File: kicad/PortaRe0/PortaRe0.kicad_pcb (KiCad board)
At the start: 4 copper layers, 135 x 77 mm, 355 parts, among them CN1 M.2, J1 StickSocket, J2 SPK_R, J3 SPK_L, J4 Battery, J6 Fan, J9 PJ-307C, Q1 BSS138, SW1 SW_START, SW2 KillSW, U1 BQ25895RTWR, U10 TPS2042BDR, U11 RP2040#2, U12 HC-USB3.0-L168-WP, U13 PCM5102APWR, U14 TPA6132A2RTER, U15 MAX98357AEWL+T_R, U16 RT9080-33GJ5, U2 TPS61023DRLR, U3 AP2112K-3.3TRG1, U4 VL812, U5 W25Q32JVSSIQ, U6 RP2040#1, U7 TPS61023DRLR, U8 USB31-TYPE-C-FSABC, U9 MAX98357AEWL+T_L, Y1 C9006, Y2 C70565, Y4 C70565

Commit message: Docs: session33終了処理・J4コネクタ確定・pcb_layout_notes作成
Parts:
- removed J4: Battery, PortaRe0:CONN-TH_S8B-PH-K-S-LF-SN
- removed K_SW65: BOOTSEL_SW, PortaRe0:KEY-SMD_4P-L4.2-W3.2-P2.20-LS4.6
- added B_SW1: BOOTSEL_SW, PortaRe0:KEY-SMD_4P-L4.2-W3.2-P2.20-LS4.6, B.Cu at (214.9, 182.4)
- added B_SW2: BOOTSEL_SW, PortaRe0:KEY-SMD_4P-L4.2-W3.2-P2.20-LS4.6, B.Cu at (222.6, 182.9)
- added SW_D64: 1N4148W, PortaRe0:SOD-123_L2.8-W1.8-LS3.7-RD, F.Cu at (241.0, 168.3)
- added Stick1: 5034800440, PortaRe0:FPC-SMD_5034800400, B.Cu at (237.7, 165.0)
- C1, C10, C100, C101, C102, C103, C104, C105, C106, C107, C108, C109, C11, C110, C111, C112, C113, C114, C115, C116, C117, C118, C119, C12, C13, C14, C15, C16, C17, C18, C19, C2, C20, C21, C22, C23, C24, C25, C26, C27, C28, C29, C3, C30, C31, C32, C33, C34, C36, C38, C4, C41, C42, C44, C46, C47, C48, C49, C5, C50, C51, C52, C53, C54, C55, C56, C57, C58, C59, C6, C60, C61, C62, C63, C64, C65, C66, C67, C68, C69, C7, C70, C71, C72, C73, C74, C75, C76, C77, C78, C79, C8, C80, C81, C82, C83, C84, C85, C86, C87, C88, C89, C9, C90, C91, C92, C93, C94, C95, C96, C97, C98, C99, CN1, D5, D6, D7, D8, D9, FPC2, FPC4, FPC5, FPC6, J2, J3, J6, J9, L1, L2, L3, L4, Q1, R1, R10, R11, R12, R13, R14, R15, R16, R17, R18, R19, R2, R20, R21, R22, R23, R24, R25, R26, R27, R28, R29, R3, R30, R31, R32, R33, R34, R35, R36, R37, R38, R39, R4, R40, R41, R42, R43, R44, R45, R46, R47, R48, R49, R5, R50, R51, R52, R53, R54, R55, R56, R57, R58, R59, R6, R60, R61, R62, R63, R64, R7, R8, R9, RP2040#1, RP2040#2, SW1, SW2, U1, U10, U11, U12, U13, U14, U15, U16, U2, U3, U4, U5, U6, U7, U8, U9, USBC1, Y1, Y2, Y4: moved to B.Cu
- J1: value StickSocket -> Battery; footprint PortaRe0:FPC-SMD_5034800400 -> PortaRe0:CONN_BM06B-ACHFKS-GACN-ETF_JST; moved to B.Cu
- K_SW64: value BOOTSEL_SW -> KeyBoard
- moved SW_D2 264.3 mm to (280.0, 108.0)
- moved K_SW17 263.2 mm to (277.0, 122.7)
- moved K_SW31 261.5 mm to (275.8, 135.5)
- moved SW_D17 257.3 mm to (277.0, 125.7), turned to 180 degrees
- moved K_SW16 256.6 mm to (268.5, 122.7)
- moved SW_D31 251.5 mm to (275.5, 138.5), turned to 180 degrees
- moved K_SW30 251.0 mm to (264.0, 131.2)
- moved K_SW15 250.1 mm to (260.0, 122.7)
- moved K_SW57 250.0 mm to (272.4, 148.2)
- moved SW_D16 249.6 mm to (268.5, 125.7), turned to 180 degrees
- moved K_SW14 243.8 mm to (251.5, 122.7)
- moved SW_D57 243.2 mm to (272.4, 151.2), turned to 180 degrees
- moved SW_D15 242.1 mm to (260.0, 125.7), turned to 180 degrees
- moved K_SW44 241.5 mm to (266.0, 139.7)
- moved SW_D30 239.8 mm to (263.8, 134.2), turned to 180 degrees
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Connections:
- J1 pad 1: GND -> +BATT
- J1 pad 2: STICK_X -> +BATT
- J1 pad 3: +3V3 -> +BATT
- J1 pad 4: STICK_Y -> GND
- J1 pad 5: (no net) -> GND
- J1 pad 6: (no net) -> GND
- K_SW1 pad 2: /keyboard/COL0 -> unconnected-(K_SW1-Pad2)
- K_SW1 pad 3: (no net) -> /keyboard/COL0
- K_SW1 pad 4: (no net) -> unconnected-(K_SW1-Pad4)
- K_SW10 pad 1: Net-(SW_D10-A) -> /keyboard/COL7
- K_SW10 pad 2: /keyboard/COL7 -> unconnected-(K_SW10-Pad2)
- K_SW10 pad 3: (no net) -> Net-(SW_D10-A)
- K_SW10 pad 4: (no net) -> unconnected-(K_SW10-Pad4)
- K_SW11 pad 1: Net-(SW_D11-A) -> /keyboard/COL8
- K_SW11 pad 2: /keyboard/COL8 -> unconnected-(K_SW11-Pad2)
- K_SW11 pad 3: (no net) -> Net-(SW_D11-A)
- K_SW11 pad 4: (no net) -> unconnected-(K_SW11-Pad4)
- K_SW12 pad 1: Net-(SW_D12-A) -> /keyboard/COL0
- K_SW12 pad 2: /keyboard/COL0 -> unconnected-(K_SW12-Pad2)
- K_SW12 pad 3: (no net) -> Net-(SW_D12-A)
- K_SW12 pad 4: (no net) -> unconnected-(K_SW12-Pad4)
- K_SW13 pad 1: Net-(SW_D13-A) -> /keyboard/COL1
- K_SW13 pad 2: /keyboard/COL1 -> unconnected-(K_SW13-Pad2)
- K_SW13 pad 3: (no net) -> Net-(SW_D13-A)
- K_SW13 pad 4: (no net) -> unconnected-(K_SW13-Pad4)
- K_SW14 pad 1: Net-(SW_D14-A) -> /keyboard/COL2
- K_SW14 pad 2: /keyboard/COL2 -> unconnected-(K_SW14-Pad2)
- K_SW14 pad 3: (no net) -> Net-(SW_D14-A)
- K_SW14 pad 4: (no net) -> unconnected-(K_SW14-Pad4)
- K_SW15 pad 1: Net-(SW_D15-A) -> /keyboard/COL3
- K_SW15 pad 2: /keyboard/COL3 -> unconnected-(K_SW15-Pad2)
- K_SW15 pad 3: (no net) -> Net-(SW_D15-A)
- K_SW15 pad 4: (no net) -> unconnected-(K_SW15-Pad4)
- K_SW16 pad 1: Net-(SW_D16-A) -> /keyboard/COL4
- K_SW16 pad 2: /keyboard/COL4 -> unconnected-(K_SW16-Pad2)
- K_SW16 pad 3: (no net) -> Net-(SW_D16-A)
- K_SW16 pad 4: (no net) -> unconnected-(K_SW16-Pad4)
- K_SW17 pad 1: Net-(SW_D17-A) -> /keyboard/COL5
- K_SW17 pad 2: /keyboard/COL5 -> unconnected-(K_SW17-Pad2)
- K_SW17 pad 3: (no net) -> Net-(SW_D17-A)
- K_SW17 pad 4: (no net) -> unconnected-(K_SW17-Pad4)
- K_SW18 pad 1: Net-(SW_D18-A) -> /keyboard/COL6
- K_SW18 pad 2: /keyboard/COL6 -> unconnected-(K_SW18-Pad2)
- K_SW18 pad 3: (no net) -> Net-(SW_D18-A)
- K_SW18 pad 4: (no net) -> unconnected-(K_SW18-Pad4)
- K_SW19 pad 1: Net-(SW_D19-A) -> /keyboard/COL7
- K_SW19 pad 2: /keyboard/COL7 -> unconnected-(K_SW19-Pad2)
- K_SW19 pad 3: (no net) -> Net-(SW_D19-A)
- K_SW19 pad 4: (no net) -> unconnected-(K_SW19-Pad4)
- K_SW2 pad 2: /keyboard/COL8 -> unconnected-(K_SW2-Pad2)
- K_SW2 pad 3: (no net) -> /keyboard/COL8
- K_SW2 pad 4: (no net) -> unconnected-(K_SW2-Pad4)
- K_SW20 pad 1: Net-(SW_D20-A) -> /keyboard/COL8
- K_SW20 pad 2: /keyboard/COL8 -> unconnected-(K_SW20-Pad2)
- K_SW20 pad 3: (no net) -> Net-(SW_D20-A)
- K_SW20 pad 4: (no net) -> unconnected-(K_SW20-Pad4)
- K_SW21 pad 1: Net-(SW_D21-A) -> /keyboard/COL0
- K_SW21 pad 2: /keyboard/COL0 -> unconnected-(K_SW21-Pad2)
- K_SW21 pad 3: (no net) -> Net-(SW_D21-A)
- K_SW21 pad 4: (no net) -> unconnected-(K_SW21-Pad4)
- K_SW22 pad 1: Net-(SW_D22-A) -> /keyboard/COL1
- K_SW22 pad 2: /keyboard/COL1 -> unconnected-(K_SW22-Pad2)
- K_SW22 pad 3: (no net) -> Net-(SW_D22-A)
- K_SW22 pad 4: (no net) -> unconnected-(K_SW22-Pad4)
- K_SW23 pad 1: Net-(SW_D23-A) -> /keyboard/COL2
- K_SW23 pad 2: /keyboard/COL2 -> unconnected-(K_SW23-Pad2)
- K_SW23 pad 3: (no net) -> Net-(SW_D23-A)
- K_SW23 pad 4: (no net) -> unconnected-(K_SW23-Pad4)
- K_SW24 pad 1: Net-(SW_D24-A) -> /keyboard/COL3
- K_SW24 pad 2: /keyboard/COL3 -> unconnected-(K_SW24-Pad2)
- K_SW24 pad 3: (no net) -> Net-(SW_D24-A)
- K_SW24 pad 4: (no net) -> unconnected-(K_SW24-Pad4)
- K_SW25 pad 1: Net-(SW_D25-A) -> /keyboard/COL4
- K_SW25 pad 2: /keyboard/COL4 -> unconnected-(K_SW25-Pad2)
- K_SW25 pad 3: (no net) -> Net-(SW_D25-A)
- K_SW25 pad 4: (no net) -> unconnected-(K_SW25-Pad4)
- K_SW26 pad 1: Net-(SW_D26-A) -> /keyboard/COL5
- K_SW26 pad 2: /keyboard/COL5 -> unconnected-(K_SW26-Pad2)
- K_SW26 pad 3: (no net) -> Net-(SW_D26-A)
- K_SW26 pad 4: (no net) -> unconnected-(K_SW26-Pad4)
- K_SW27 pad 1: Net-(SW_D27-A) -> /keyboard/COL6
- K_SW27 pad 2: /keyboard/COL6 -> unconnected-(K_SW27-Pad2)
- K_SW27 pad 3: (no net) -> Net-(SW_D27-A)
- K_SW27 pad 4: (no net) -> unconnected-(K_SW27-Pad4)
- K_SW28 pad 1: Net-(SW_D28-A) -> /keyboard/COL7
- K_SW28 pad 2: /keyboard/COL7 -> unconnected-(K_SW28-Pad2)
- K_SW28 pad 3: (no net) -> Net-(SW_D28-A)
- K_SW28 pad 4: (no net) -> unconnected-(K_SW28-Pad4)
- K_SW29 pad 1: Net-(SW_D29-A) -> /keyboard/COL8
- K_SW29 pad 2: /keyboard/COL8 -> unconnected-(K_SW29-Pad2)
- K_SW29 pad 3: (no net) -> Net-(SW_D29-A)
- K_SW29 pad 4: (no net) -> unconnected-(K_SW29-Pad4)
- K_SW3 pad 1: Net-(SW_D3-A) -> /keyboard/COL0
- K_SW3 pad 2: /keyboard/COL0 -> unconnected-(K_SW3-Pad2)
- K_SW3 pad 3: (no net) -> Net-(SW_D3-A)
- K_SW3 pad 4: (no net) -> unconnected-(K_SW3-Pad4)
- K_SW30 pad 1: Net-(SW_D30-A) -> /keyboard/COL0
- K_SW30 pad 2: /keyboard/COL0 -> unconnected-(K_SW30-Pad2)
- K_SW30 pad 3: (no net) -> Net-(SW_D30-A)
- K_SW30 pad 4: (no net) -> unconnected-(K_SW30-Pad4)
- K_SW31 pad 1: Net-(SW_D31-A) -> /keyboard/COL1
- K_SW31 pad 2: /keyboard/COL1 -> unconnected-(K_SW31-Pad2)
- K_SW31 pad 3: (no net) -> Net-(SW_D31-A)
- K_SW31 pad 4: (no net) -> unconnected-(K_SW31-Pad4)
- K_SW32 pad 1: Net-(SW_D32-A) -> /keyboard/COL2
- K_SW32 pad 2: /keyboard/COL2 -> unconnected-(K_SW32-Pad2)
- K_SW32 pad 3: (no net) -> Net-(SW_D32-A)
- K_SW32 pad 4: (no net) -> unconnected-(K_SW32-Pad4)
- K_SW33 pad 1: Net-(SW_D33-A) -> /keyboard/COL3
- K_SW33 pad 2: /keyboard/COL3 -> unconnected-(K_SW33-Pad2)
- K_SW33 pad 3: (no net) -> Net-(SW_D33-A)
- K_SW33 pad 4: (no net) -> unconnected-(K_SW33-Pad4)
- K_SW34 pad 1: Net-(SW_D34-A) -> /keyboard/COL4
- K_SW34 pad 2: /keyboard/COL4 -> unconnected-(K_SW34-Pad2)
- K_SW34 pad 3: (no net) -> Net-(SW_D34-A)
- K_SW34 pad 4: (no net) -> unconnected-(K_SW34-Pad4)
- K_SW35 pad 1: Net-(SW_D35-A) -> /keyboard/COL5
- K_SW35 pad 2: /keyboard/COL5 -> unconnected-(K_SW35-Pad2)
- K_SW35 pad 3: (no net) -> Net-(SW_D35-A)
- K_SW35 pad 4: (no net) -> unconnected-(K_SW35-Pad4)
- K_SW36 pad 1: Net-(SW_D36-A) -> /keyboard/COL6
- K_SW36 pad 2: /keyboard/COL6 -> unconnected-(K_SW36-Pad2)
- K_SW36 pad 3: (no net) -> Net-(SW_D36-A)
- K_SW36 pad 4: (no net) -> unconnected-(K_SW36-Pad4)
- K_SW37 pad 1: Net-(SW_D37-A) -> /keyboard/COL7
- K_SW37 pad 2: /keyboard/COL7 -> unconnected-(K_SW37-Pad2)
- K_SW37 pad 3: (no net) -> Net-(SW_D37-A)
- K_SW37 pad 4: (no net) -> unconnected-(K_SW37-Pad4)
- K_SW38 pad 1: Net-(SW_D38-A) -> /keyboard/COL8
- K_SW38 pad 2: /keyboard/COL8 -> unconnected-(K_SW38-Pad2)
- K_SW38 pad 3: (no net) -> Net-(SW_D38-A)
- K_SW38 pad 4: (no net) -> unconnected-(K_SW38-Pad4)
- K_SW39 pad 1: Net-(SW_D39-A) -> /keyboard/COL0
- K_SW39 pad 2: /keyboard/COL0 -> unconnected-(K_SW39-Pad2)
- K_SW39 pad 3: (no net) -> Net-(SW_D39-A)
- K_SW39 pad 4: (no net) -> unconnected-(K_SW39-Pad4)
- K_SW4 pad 1: Net-(SW_D4-A) -> /keyboard/COL1
- K_SW4 pad 2: /keyboard/COL1 -> unconnected-(K_SW4-Pad2)
- K_SW4 pad 3: (no net) -> Net-(SW_D4-A)
- K_SW4 pad 4: (no net) -> unconnected-(K_SW4-Pad4)
- K_SW40 pad 1: Net-(SW_D40-A) -> /keyboard/COL1
- K_SW40 pad 2: /keyboard/COL1 -> unconnected-(K_SW40-Pad2)
- K_SW40 pad 3: (no net) -> Net-(SW_D40-A)
- K_SW40 pad 4: (no net) -> unconnected-(K_SW40-Pad4)
- K_SW41 pad 1: Net-(SW_D41-A) -> /keyboard/COL2
- K_SW41 pad 2: /keyboard/COL2 -> unconnected-(K_SW41-Pad2)
- K_SW41 pad 3: (no net) -> Net-(SW_D41-A)
- K_SW41 pad 4: (no net) -> unconnected-(K_SW41-Pad4)
- K_SW42 pad 1: Net-(SW_D42-A) -> /keyboard/COL3
- K_SW42 pad 2: /keyboard/COL3 -> unconnected-(K_SW42-Pad2)
- K_SW42 pad 3: (no net) -> Net-(SW_D42-A)
- K_SW42 pad 4: (no net) -> unconnected-(K_SW42-Pad4)
- K_SW43 pad 1: Net-(SW_D43-A) -> /keyboard/COL4
- K_SW43 pad 2: /keyboard/COL4 -> unconnected-(K_SW43-Pad2)
- K_SW43 pad 3: (no net) -> Net-(SW_D43-A)
- K_SW43 pad 4: (no net) -> unconnected-(K_SW43-Pad4)
- K_SW44 pad 1: Net-(SW_D44-A) -> /keyboard/COL5
- K_SW44 pad 2: /keyboard/COL5 -> unconnected-(K_SW44-Pad2)
- K_SW44 pad 3: (no net) -> Net-(SW_D44-A)
- K_SW44 pad 4: (no net) -> unconnected-(K_SW44-Pad4)
- K_SW45 pad 1: Net-(SW_D45-A) -> /keyboard/COL6
- K_SW45 pad 2: /keyboard/COL6 -> unconnected-(K_SW45-Pad2)
- K_SW45 pad 3: (no net) -> Net-(SW_D45-A)
- K_SW45 pad 4: (no net) -> unconnected-(K_SW45-Pad4)
- K_SW46 pad 1: Net-(SW_D46-A) -> /keyboard/COL7
- K_SW46 pad 2: /keyboard/COL7 -> unconnected-(K_SW46-Pad2)
- K_SW46 pad 3: (no net) -> Net-(SW_D46-A)
- K_SW46 pad 4: (no net) -> unconnected-(K_SW46-Pad4)
- K_SW47 pad 1: Net-(SW_D47-A) -> /keyboard/COL8
- K_SW47 pad 2: /keyboard/COL8 -> unconnected-(K_SW47-Pad2)
- K_SW47 pad 3: (no net) -> Net-(SW_D47-A)
- K_SW47 pad 4: (no net) -> unconnected-(K_SW47-Pad4)
- K_SW48 pad 1: Net-(SW_D48-A) -> /keyboard/COL0
- K_SW48 pad 2: /keyboard/COL0 -> unconnected-(K_SW48-Pad2)
- K_SW48 pad 3: (no net) -> Net-(SW_D48-A)
- K_SW48 pad 4: (no net) -> unconnected-(K_SW48-Pad4)
- K_SW49 pad 1: Net-(SW_D49-A) -> /keyboard/COL1
- K_SW49 pad 2: /keyboard/COL1 -> unconnected-(K_SW49-Pad2)
- K_SW49 pad 3: (no net) -> Net-(SW_D49-A)
- K_SW49 pad 4: (no net) -> unconnected-(K_SW49-Pad4)
- K_SW5 pad 1: Net-(SW_D5-A) -> /keyboard/COL2
- K_SW5 pad 2: /keyboard/COL2 -> unconnected-(K_SW5-Pad2)
- K_SW5 pad 3: (no net) -> Net-(SW_D5-A)
- K_SW5 pad 4: (no net) -> unconnected-(K_SW5-Pad4)
- K_SW50 pad 1: Net-(SW_D50-A) -> /keyboard/COL2
- K_SW50 pad 2: /keyboard/COL2 -> unconnected-(K_SW50-Pad2)
- K_SW50 pad 3: (no net) -> Net-(SW_D50-A)
- K_SW50 pad 4: (no net) -> unconnected-(K_SW50-Pad4)
- K_SW51 pad 1: Net-(SW_D51-A) -> /keyboard/COL3
- K_SW51 pad 2: /keyboard/COL3 -> unconnected-(K_SW51-Pad2)
- K_SW51 pad 3: (no net) -> Net-(SW_D51-A)
- K_SW51 pad 4: (no net) -> unconnected-(K_SW51-Pad4)
- K_SW52 pad 1: Net-(SW_D52-A) -> /keyboard/COL4
- K_SW52 pad 2: /keyboard/COL4 -> unconnected-(K_SW52-Pad2)
- K_SW52 pad 3: (no net) -> Net-(SW_D52-A)
- K_SW52 pad 4: (no net) -> unconnected-(K_SW52-Pad4)
- K_SW53 pad 1: Net-(SW_D53-A) -> /keyboard/COL5
- K_SW53 pad 2: /keyboard/COL5 -> unconnected-(K_SW53-Pad2)
- K_SW53 pad 3: (no net) -> Net-(SW_D53-A)
- K_SW53 pad 4: (no net) -> unconnected-(K_SW53-Pad4)
- K_SW54 pad 1: Net-(SW_D54-A) -> /keyboard/COL6
- K_SW54 pad 2: /keyboard/COL6 -> unconnected-(K_SW54-Pad2)
- K_SW54 pad 3: (no net) -> Net-(SW_D54-A)
- K_SW54 pad 4: (no net) -> unconnected-(K_SW54-Pad4)
- K_SW55 pad 1: Net-(SW_D55-A) -> /keyboard/COL7
- K_SW55 pad 2: /keyboard/COL7 -> unconnected-(K_SW55-Pad2)
- K_SW55 pad 3: (no net) -> Net-(SW_D55-A)
- K_SW55 pad 4: (no net) -> unconnected-(K_SW55-Pad4)
- K_SW56 pad 1: Net-(SW_D56-A) -> /keyboard/COL8
- K_SW56 pad 2: /keyboard/COL8 -> unconnected-(K_SW56-Pad2)
- K_SW56 pad 3: (no net) -> Net-(SW_D56-A)
- K_SW56 pad 4: (no net) -> unconnected-(K_SW56-Pad4)
- K_SW57 pad 1: Net-(SW_D57-A) -> /keyboard/COL0
- K_SW57 pad 2: /keyboard/COL0 -> unconnected-(K_SW57-Pad2)
- K_SW57 pad 3: (no net) -> Net-(SW_D57-A)
- K_SW57 pad 4: (no net) -> unconnected-(K_SW57-Pad4)
- K_SW58 pad 1: Net-(SW_D58-A) -> /keyboard/COL1
- K_SW58 pad 2: /keyboard/COL1 -> unconnected-(K_SW58-Pad2)
- K_SW58 pad 3: (no net) -> Net-(SW_D58-A)
- K_SW58 pad 4: (no net) -> unconnected-(K_SW58-Pad4)
- K_SW59 pad 1: Net-(SW_D59-A) -> /keyboard/COL2
- K_SW59 pad 2: /keyboard/COL2 -> unconnected-(K_SW59-Pad2)
- K_SW59 pad 3: (no net) -> Net-(SW_D59-A)
- K_SW59 pad 4: (no net) -> unconnected-(K_SW59-Pad4)
- K_SW6 pad 1: Net-(SW_D6-A) -> /keyboard/COL3
- K_SW6 pad 2: /keyboard/COL3 -> unconnected-(K_SW6-Pad2)
- K_SW6 pad 3: (no net) -> Net-(SW_D6-A)
- K_SW6 pad 4: (no net) -> unconnected-(K_SW6-Pad4)
- K_SW60 pad 1: Net-(SW_D60-A) -> /keyboard/COL3
- K_SW60 pad 2: /keyboard/COL3 -> unconnected-(K_SW60-Pad2)
- K_SW60 pad 3: (no net) -> Net-(SW_D60-A)
- K_SW60 pad 4: (no net) -> unconnected-(K_SW60-Pad4)
- K_SW61 pad 1: Net-(SW_D61-A) -> /keyboard/COL4
- K_SW61 pad 2: /keyboard/COL4 -> unconnected-(K_SW61-Pad2)
- K_SW61 pad 3: (no net) -> Net-(SW_D61-A)
- K_SW61 pad 4: (no net) -> unconnected-(K_SW61-Pad4)
- K_SW62 pad 1: Net-(SW_D62-A) -> /keyboard/COL5
- K_SW62 pad 2: /keyboard/COL5 -> unconnected-(K_SW62-Pad2)
- K_SW62 pad 3: (no net) -> Net-(SW_D62-A)
- K_SW62 pad 4: (no net) -> unconnected-(K_SW62-Pad4)
- K_SW63 pad 1: Net-(SW_D63-A) -> /keyboard/COL6
- K_SW63 pad 2: /keyboard/COL6 -> unconnected-(K_SW63-Pad2)
- K_SW63 pad 3: (no net) -> Net-(SW_D63-A)
- K_SW63 pad 4: (no net) -> unconnected-(K_SW63-Pad4)
- K_SW64 pad 1: GND -> /keyboard/COL7
- K_SW64 pad 2: /keyboard/QSPI_SS -> unconnected-(K_SW64-Pad2)
- K_SW64 pad 3: (no net) -> Net-(SW_D64-A)
- K_SW64 pad 4: (no net) -> unconnected-(K_SW64-Pad4)
- K_SW7 pad 1: Net-(SW_D7-A) -> /keyboard/COL4
- K_SW7 pad 2: /keyboard/COL4 -> unconnected-(K_SW7-Pad2)
- K_SW7 pad 3: (no net) -> Net-(SW_D7-A)
- K_SW7 pad 4: (no net) -> unconnected-(K_SW7-Pad4)
- K_SW8 pad 1: Net-(SW_D8-A) -> /keyboard/COL5
- K_SW8 pad 2: /keyboard/COL5 -> unconnected-(K_SW8-Pad2)
- K_SW8 pad 3: (no net) -> Net-(SW_D8-A)
- K_SW8 pad 4: (no net) -> unconnected-(K_SW8-Pad4)
- K_SW9 pad 1: Net-(SW_D9-A) -> /keyboard/COL6
- K_SW9 pad 2: /keyboard/COL6 -> unconnected-(K_SW9-Pad2)
- K_SW9 pad 3: (no net) -> Net-(SW_D9-A)
- K_SW9 pad 4: (no net) -> unconnected-(K_SW9-Pad4)
- SW1 pad 1: VSYS -> Net-(D8-A)
- SW1 pad 2: Net-(D8-A) -> unconnected-(SW1-Pad2)
- SW1 pad 3: (no net) -> VSYS
- SW1 pad 4: (no net) -> unconnected-(SW1-Pad4)
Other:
- outline, holes or cut-outs redrawn
- copper layers 4 -> 6

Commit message: Docs: session34終了処理・0402化確定・ディスプレイ調査・PCBレイアウト進行中
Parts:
- C100, C101, C103, C105, C106, C11, C111, C112, C114, C115, C116, C117, C118, C119, C12, C14, C15, C16, C17, C18, C19, C2, C20, C21, C22, C23, C24, C25, C26, C27, C28, C29, C30, C31, C32, C33, C34, C36, C38, C4, C41, C42, C44, C46, C47, C48, C49, C5, C50, C51, C52, C53, C54, C55, C56, C57, C58, C59, C60, C61, C62, C63, C64, C65, C66, C67, C68, C69, C7, C71, C72, C74, C75, C76, C77, C78, C79, C80, C81, C82, C83, C84, C85, C86, C87, C88, C89, C9, C90, C91, C92, C93, C94, C95, C96, C97, C98, C99: footprint Capacitor_SMD:C_0603_1608Metric -> Capacitor_SMD:C_0402_1005Metric
- R1, R10, R11, R12, R13, R14, R15, R16, R17, R19, R2, R20, R21, R22, R23, R24, R25, R26, R29, R3, R30, R31, R32, R33, R34, R36, R37, R38, R39, R4, R42, R43, R44, R46, R47, R48, R49, R52, R53, R54, R55, R56, R57, R58, R59, R6, R60, R61, R62, R63, R64, R7, R8: footprint Resistor_SMD:R_0603_1608Metric -> Resistor_SMD:R_0402_1005Metric
- moved R62 195.1 mm to (270.7, 139.0)
- moved C31 194.3 mm to (272.0, 143.2), turned to -90 degrees
- moved C33 193.1 mm to (270.5, 140.8)
- moved C27 193.0 mm to (283.0, 126.8), turned to 90 degrees
- moved C21 190.5 mm to (281.5, 126.8), turned to 90 degrees
- moved C29 189.0 mm to (278.3, 124.8)
- moved R61 178.2 mm to (244.4, 147.8)
- moved R39 165.1 mm to (255.5, 129.4)
- moved R63 164.3 mm to (252.2, 126.2), turned to -90 degrees
- moved R52 162.6 mm to (221.7, 150.5)
- moved R53 162.6 mm to (221.7, 148.0)
- moved R56 162.6 mm to (221.7, 143.0)
- moved R57 162.6 mm to (221.7, 140.5)
- moved R55 162.6 mm to (221.7, 145.5)
- moved R60 162.6 mm to (221.7, 137.9)
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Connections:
- J1 pad 10: GND -> (no net)
- J1 pad 7: GND -> (no net)
- J1 pad 8: GND -> (no net)
- J1 pad 9: GND -> (no net)

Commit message: Docs: session35終了処理・TPS61023 FB接続ミス確認・M.2クリアランス1.1mm
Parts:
- removed C111: 10μF, Capacitor_SMD:C_0402_1005Metric
- moved C77 202.6 mm to (273.7, 127.5)
- moved C89 193.8 mm to (269.3, 119.8), turned to 180 degrees
- moved C99 189.7 mm to (269.3, 118.8), turned to 180 degrees
- moved C78 188.6 mm to (257.9, 127.3), turned to 180 degrees
- moved C75 187.8 mm to (260.2, 126.4)
- moved C74 186.2 mm to (260.9, 121.3), turned to 180 degrees
- moved C93 184.6 mm to (269.3, 115.8)
- moved C91 182.8 mm to (269.4, 112.8), turned to 180 degrees
- moved C92 182.3 mm to (267.8, 115.1), turned to -90 degrees
- moved R8 182.3 mm to (269.3, 116.8), turned to 180 degrees
- moved C71 181.6 mm to (236.1, 173.0)
- moved C84 181.1 mm to (257.9, 126.4), turned to 180 degrees
- moved R37 180.7 mm to (261.4, 127.5), turned to 180 degrees
- moved C70 180.7 mm to (235.8, 174.2)
- moved C79 178.8 mm to (246.1, 127.7)
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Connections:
- R45 pad 1: 5V_SYS -> /usb_hub/HUB_5V

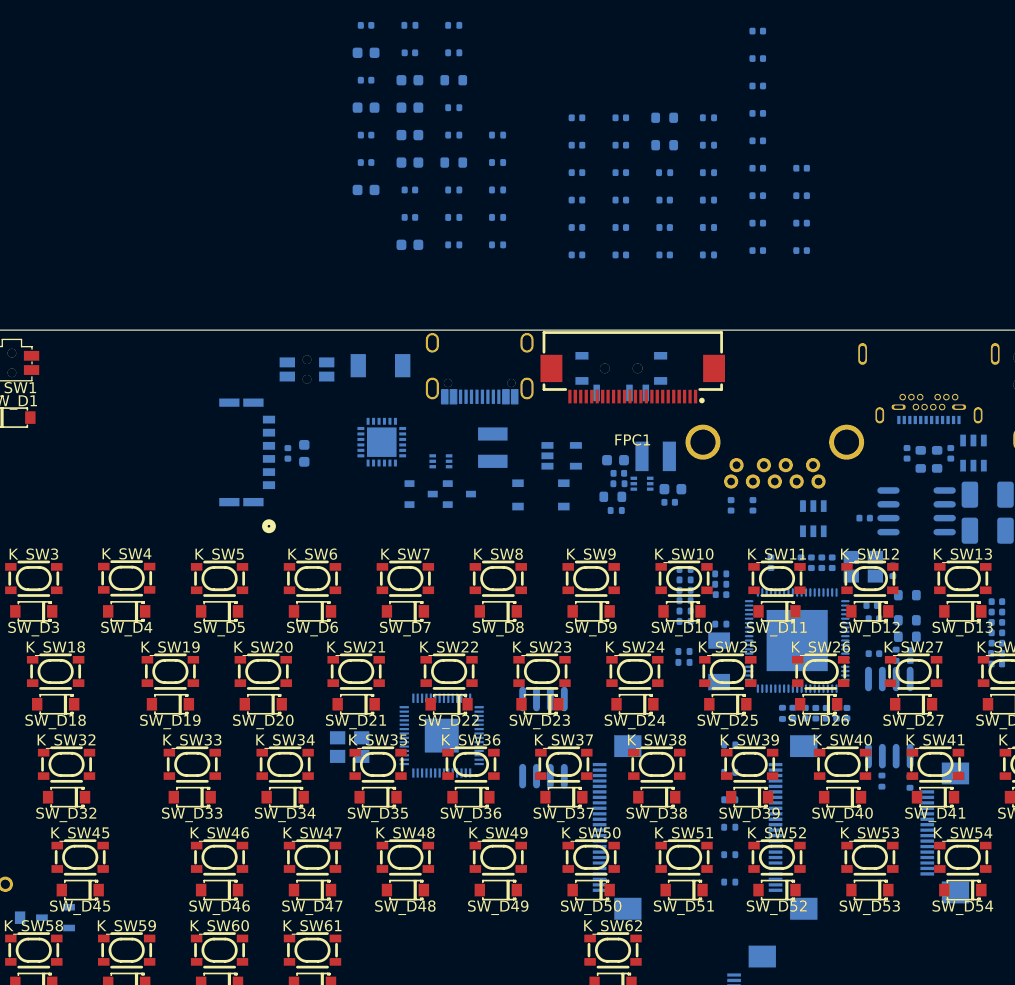
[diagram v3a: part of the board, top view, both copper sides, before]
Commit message: Docs: session36終了処理・VL812受動部品配置方針確定
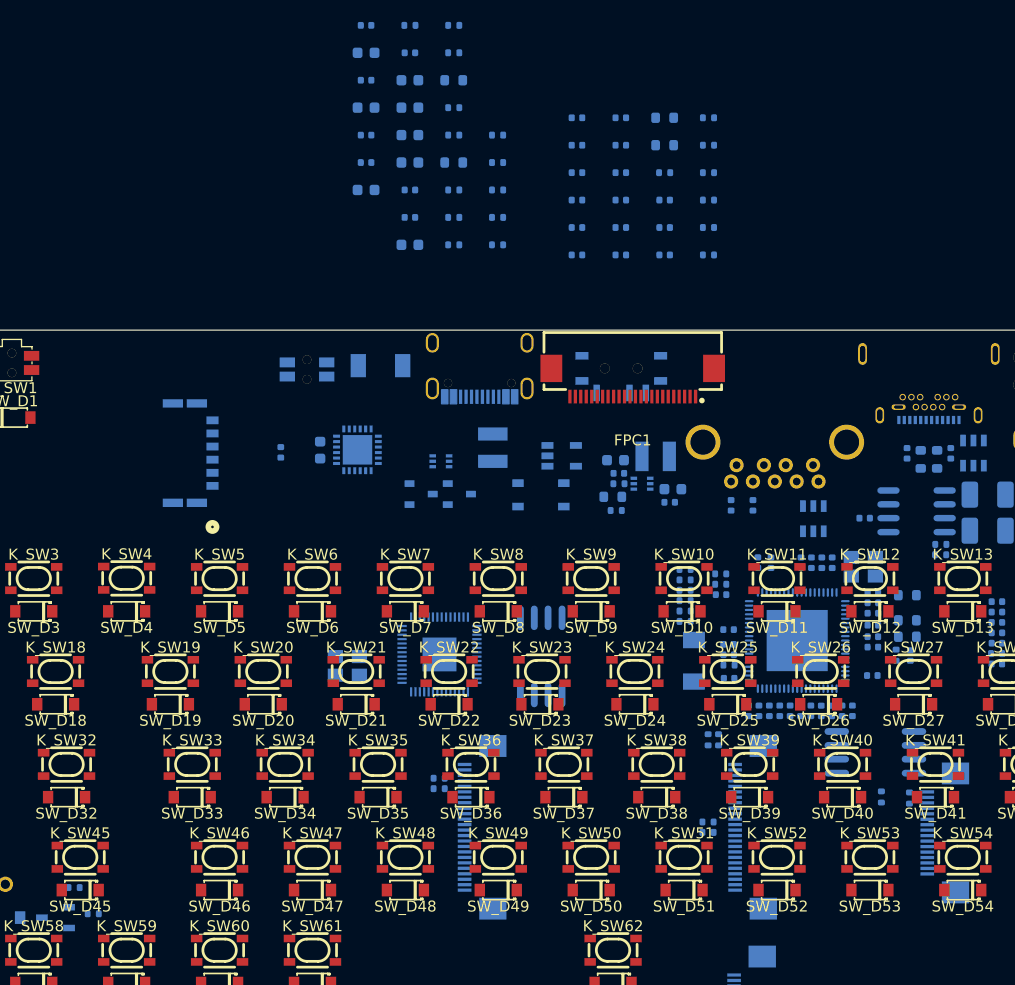
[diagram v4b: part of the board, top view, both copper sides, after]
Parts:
- added C111: 10μF, Capacitor_SMD:C_0402_1005Metric, B.Cu at (231.9, 134.8)
- moved C23 62.2 mm to (225.3, 134.8), turned to 90 degrees
- moved R56 60.5 mm to (161.7, 151.0)
- moved R57 59.7 mm to (163.4, 153.4)
- moved C18 52.2 mm to (227.2, 134.8), turned to 90 degrees
- moved C20 52.1 mm to (221.6, 129.7)
- moved C17 49.7 mm to (226.2, 134.8), turned to 90 degrees
- moved C19 48.7 mm to (221.6, 128.8)
- moved C16 47.1 mm to (224.3, 134.8), turned to 90 degrees
- moved C22 46.1 mm to (224.2, 121.3), turned to -90 degrees
- moved C15 44.6 mm to (223.4, 134.8), turned to 90 degrees
- moved C28 43.4 mm to (234.8, 128.1), turned to 180 degrees
- moved C14 40.3 mm to (234.7, 131.6), turned to 180 degrees
- moved C24 39.7 mm to (221.6, 131.8)
- moved C26 38.8 mm to (234.8, 125.9), turned to 180 degrees
- moved C25 37.8 mm to (221.6, 127.4)
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
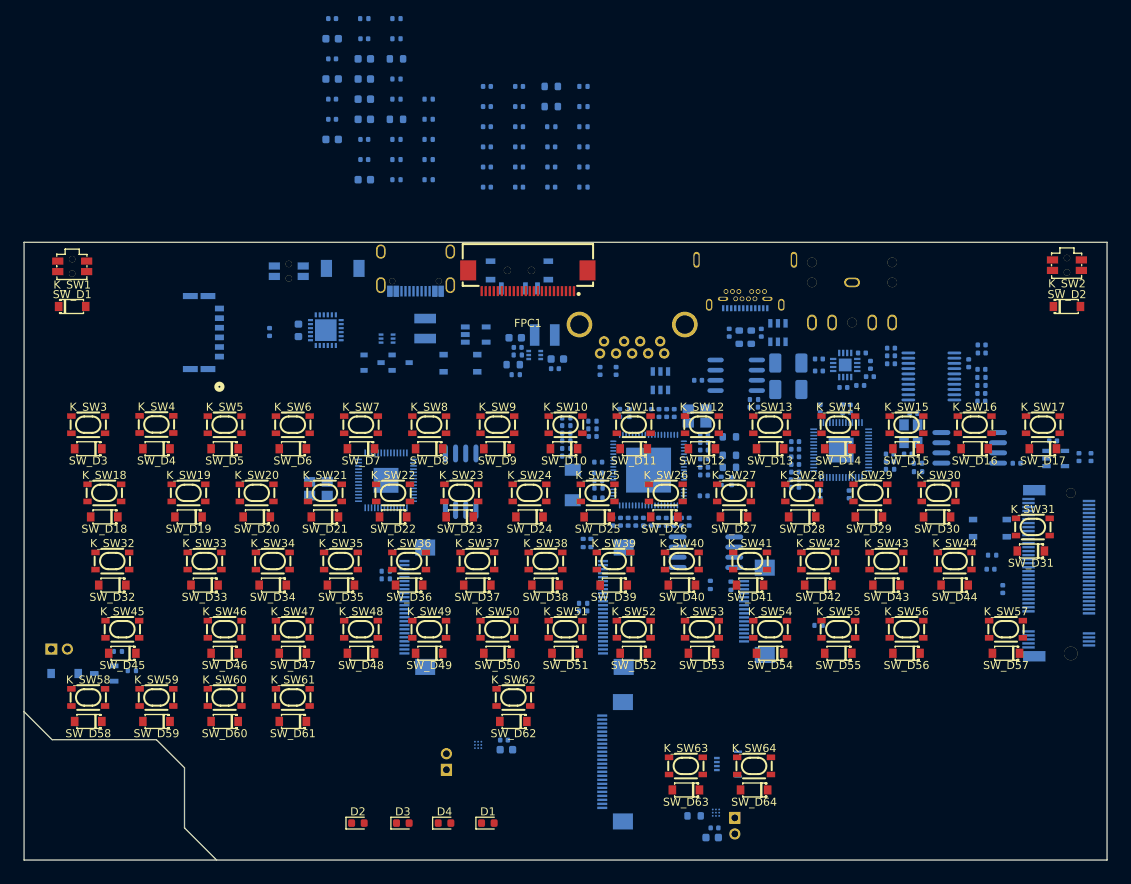
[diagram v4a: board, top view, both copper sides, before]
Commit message: Docs: session37終了処理・部品配置完了・ルーティング開始・FPC給電ピン修正
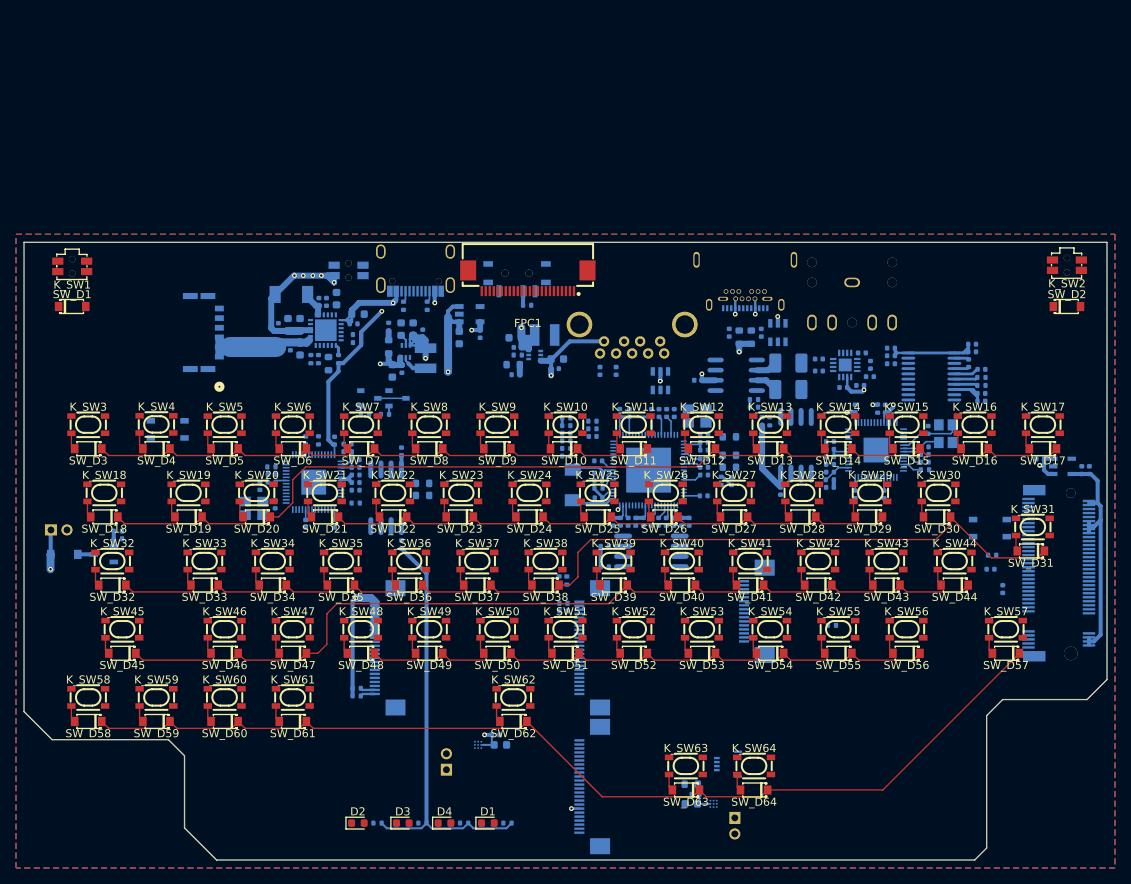
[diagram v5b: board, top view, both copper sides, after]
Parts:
- R53, R55: value 22kΩ -> 10kΩ
- moved R33 90.5 mm to (204.9, 172.4)
- moved R32 89.1 mm to (199.7, 172.4)
- moved R31 88.1 mm to (194.1, 172.4)
- moved R3 83.9 mm to (210.3, 172.4), turned to 180 degrees
- moved C64 57.4 mm to (180.9, 128.9)
- moved R26 54.9 mm to (180.8, 128.0), turned to 180 degrees
- moved C68 54.4 mm to (181.3, 132.7), turned to -90 degrees
- moved R34 54.2 mm to (190.3, 126.1)
- moved C65 52.0 mm to (179.4, 130.4), turned to 90 degrees
- moved C56 52.0 mm to (191.3, 129.9), turned to 180 degrees
- moved R28 52.0 mm to (199.7, 130.1)
- moved C63 52.0 mm to (191.3, 130.9), turned to 180 degrees
- moved R27 51.1 mm to (199.7, 131.6)
- moved R30 50.6 mm to (191.3, 132.5), turned to 180 degrees
- moved R29 50.0 mm to (197.1, 137.7), turned to -90 degrees
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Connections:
- FPC4 pad 1: GND -> 5V_SYS
- FPC4 pad 10: GND -> 5V_SYS
- FPC4 pad 23: GND -> Net-(FPC4-Pad23)
- FPC4 pad 24: GND -> Net-(FPC4-Pad24)
- FPC4 pad 3: GND -> 5V_SYS
- FPC4 pad 4: Net-(FPC4-Pad4) -> 5V_SYS
- FPC4 pad 5: Net-(FPC4-Pad5) -> 5V_SYS
- FPC4 pad 6: GND -> 5V_SYS
- FPC4 pad 7: GND -> 5V_SYS
- FPC4 pad 8: GND -> 5V_SYS
- FPC4 pad 9: GND -> 5V_SYS
- R53 pad 2: Net-(FPC4-Pad5) -> Net-(FPC4-Pad24)
- R55 pad 2: Net-(FPC4-Pad4) -> Net-(FPC4-Pad23)
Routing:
- net 5V_SYS: track 0.00 -> 267.9 mm, vias 0 -> 8
- net +3V3: track 0.00 -> 165.1 mm, vias 0 -> 6
- net /keyboard/ROW7: track 0.00 -> 129.2 mm
- net /keyboard/ROW2: track 0.00 -> 127.2 mm
- net /keyboard/ROW4: track 0.00 -> 127.1 mm
- net /keyboard/ROW5: track 0.00 -> 114.4 mm
- net VSYS: track 0.00 -> 76.4 mm, vias 0 -> 7
- net /keyboard/ROW6: track 0.00 -> 73.6 mm
- net /keyboard/ROW1: track 0.00 -> 73.6 mm
- net /keyboard/ROW3: track 0.00 -> 73.4 mm
- net /usb_hub/HUB_5V: track 0.00 -> 73.1 mm, vias 0 -> 7
- net 1V2_HUB: track 0.00 -> 34.4 mm
- net /m2_ssd/3V3_M2: track 0.00 -> 32.7 mm
- net 3V3_HUB: track 0.00 -> 24.2 mm
- net VBUS: track 0.00 -> 19.3 mm, vias 0 -> 2
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- added copper zone on B.Cu, net GND
- added copper zone on F.Cu, net GND
- added copper zone on In1.Cu, net GND
- added copper zone on In2.Cu, net GND
- added copper zone on In3.Cu, net GND
- added copper zone on In4.Cu, net GND
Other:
- outline, holes or cut-outs redrawn
